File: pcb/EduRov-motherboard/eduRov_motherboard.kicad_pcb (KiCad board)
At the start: 4 copper layers, 167.7 x 124.6 mm, 65 parts, among them IC201 L6203, IC301 L6203, IC401 L6203, IC501 L6203, P101 Battery connector, P102 Ext press, P103 Ext temp, Q101 IRL540NPBF, U201 ACS723xLCTR-05AB, U301 ACS723xLCTR-05AB, U401 ACS723xLCTR-05AB, U501 ACS723xLCTR-05AB

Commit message: Update PCBs after prototyping
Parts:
- removed 2Pscrew105: Ch LED, Connectors_Terminal_Blocks:TerminalBlock_Altech_AK300-2_P5.00mm
- added P104: Ext press, Connector_JST:JST_PH_B4B-PH-K_1x04_P2.00mm_Vertical, F.Cu at (174.2, 139.1)
- added P105: Ch LED, Connector_JST:JST_PH_B4B-PH-K_1x04_P2.00mm_Vertical, F.Cu at (63.6, 87.9)
- 2Pscrew101, 2Pscrew102, 2Pscrew103, 2Pscrew104: footprint Connectors_Terminal_Blocks:TerminalBlock_Altech_AK300-2_P5.00mm -> TerminalBlock_Altech:Altech_AK300_1x02_P5.00mm_45-Degree
- IC201, IC301, IC401, IC501: footprint EduROV:MULTIWATT-11 -> SnapEDA Library:MULTIWATT-11
- P102: footprint Connectors_Terminal_Blocks:TerminalBlock_Altech_AK300-3_P5.00mm -> Connector_JST:JST_PH_B3B-PH-K_1x03_P2.00mm_Vertical
- P103: value Ext temp -> Ext press; footprint Connectors_Terminal_Blocks:TerminalBlock_Altech_AK300-3_P5.00mm -> Connector_JST:JST_PH_B3B-PH-K_1x03_P2.00mm_Vertical
- Q101: footprint TO_SOT_Packages_THT:TO-220-3_Vertical -> Package_TO_SOT_THT:TO-220-3_Vertical
- moved P103 18.4 mm to (174.2, 120.6)
- moved P102 13.5 mm to (174.2, 105.4)
- moved Q101 10.4 mm to (69.7, 82.1)
- moved D502 9.17 mm to (75.3, 40.1), turned to 270 degrees
- moved C203 8.51 mm to (209.4, 64.2), turned to 90 degrees
- moved 2Pscrew104 5.02 mm to (197.8, 46.4), turned to 90 degrees
- moved 2Pscrew101 5.02 mm to (83.8, 46.4), turned to 90 degrees
- moved 2Pscrew102 5.02 mm to (121.9, 46.4), turned to 90 degrees
- moved 2Pscrew103 5.02 mm to (159.8, 46.4), turned to 90 degrees
- moved C102 4.15 mm to (64.2, 77.5), turned to 0 degrees
- moved D501 1.61 mm to (74.9, 48.1), turned to 225 degrees
- moved R105 1.60 mm to (64.3, 71.7)
- moved R108 0.13 mm to (134.6, 74.7)
- renumbered C107 to C102
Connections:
- 2Pscrew101 pad 1: /Mot1+ -> /Mot1-
- 2Pscrew101 pad 2: /Mot1- -> /Mot1+
- 2Pscrew102 pad 1: /Mot2+ -> /Mot2-
- 2Pscrew102 pad 2: /Mot2- -> /Mot2+
- 2Pscrew103 pad 1: /Mot3+ -> /Mot3-
- 2Pscrew103 pad 2: /Mot3- -> /Mot3+
- 2Pscrew104 pad 1: /Mot4+ -> /Mot4-
- 2Pscrew104 pad 2: /Mot4- -> /Mot4+
- P101 pad 1: +Bat -> Net-(P101-Pad1)
- P101 pad 2: -Batt -> Net-(P101-Pad2)
- RaspberryPI101 pad 1: Net-(RaspberryPI101-Pad1) -> +3V3
- RaspberryPI101 pad 17: Net-(RaspberryPI101-Pad17) -> +3V3
- RaspberryPI101 pad 3: Net-(RaspberryPI101-Pad3) -> SCL
- RaspberryPI101 pad 5: Net-(RaspberryPI101-Pad5) -> SDA
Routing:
- net +3V3: track 0.00 -> 110.5 mm
- net SCL: track 0.00 -> 108.3 mm
- net SDA: track 0.00 -> 104.9 mm
- net IO_LED: track 20.2 -> 40.3 mm
- net TempMonitor: track 120.1 -> 103.1 mm
- net +Bat: track 57.6 -> 69.2 mm
- net PressMonitor: track 105.1 -> 94.2 mm
- net IO1A: track 58.7 -> 50.4 mm
- net IO1B: track 55.7 -> 49.2 mm
- net IOEN: track 188.6 -> 185.3 mm
- net /Mot1+: track 43.3 -> 46.4 mm
- net Net-(P105-Pad1): track 14.5 -> 11.6 mm
- net /Mot1-: track 27.5 -> 28.4 mm
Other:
- outline, holes or cut-outs redrawn
- board text added: "3V3 SCL SDA GND"
- board text added: "5V SIG GND"
- board text added: "Headlights"
- board text added: "I2C"
- board text added: "Revision by: Simen August Tinderholt 02.01.2020"
- board text added: "Temp"
- board text added: "V+ GND V+ GND"
- board text added: "eduROV motherboard v0.4 www.edurov.no"
- board text removed: "5V"
- board text removed: "GND"
- board text removed: "LED Channel"
- board text removed: "Revision by: Simen August Tinderholt 28.02.2020"
- board text removed: "Sig"
- board text removed: "Temperature"
- board text removed: "eduROV motherboard v0.5 www.edurov.no"

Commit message: Update schematic.
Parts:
- removed R106: 0, Resistor_THT:R_Axial_DIN0204_L3.6mm_D1.6mm_P1.90mm_Vertical
- RaspberryPI101: footprint EduROV:RaspBerry_PI -> EduRov:RaspBerry_PI
- moved R112 39.9 mm to (63.4, 89.2), turned to 0 degrees
- moved R105 20.6 mm to (63.4, 92.3)
- moved P105 13.3 mm to (61.7, 74.7), turned to 270 degrees
- moved R111 10.4 mm to (134.4, 85.1), turned to 90 degrees
- moved R108 8.96 mm to (143.6, 74.9), turned to 270 degrees
- moved R109 8.51 mm to (140.5, 85.1), turned to 90 degrees
- moved R110 6.50 mm to (137.5, 74.9), turned to 270 degrees
- moved C102 6.32 mm to (69.5, 74.0)
- moved P101 3.50 mm to (199.8, 80.5)
- moved Q101 3.39 mm to (69.3, 78.7)
- renumbered R107 to R112
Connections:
- A101 pad 17: Net-(A101-Pad17) -> +3V3
- A101 pad 19: Sense4 -> TempMonitor
- A101 pad 20: Sense3 -> PressMonitor
- A101 pad 21: Sense2 -> BattMonitor
- A101 pad 22: Sense1 -> Net-(A101-Pad22)
- A101 pad 23: Net-(A101-Pad23) -> Sense4
- A101 pad 24: BattMonitor -> Sense3
- A101 pad 25: PressMonitor -> Sense2
- A101 pad 26: TempMonitor -> Sense1
- A101 pad 27: Net-(A101-Pad27) -> +5V
- P101 pad 2: Net-(P101-Pad2) -> -Batt
- P102 pad 1: +5V -> PressMonitor
- P102 pad 2: PressMonitor -> +5V
- P103 pad 1: +5V -> TempMonitor
- P103 pad 2: TempMonitor -> +5V
- P104 pad 1: +3V3 -> SCL
- P104 pad 3: SCL -> +3V3
- P105 pad 1: Net-(P105-Pad1) -> +Bat
- P105 pad 2: +Bat -> LED-
- P105 pad 3: Net-(P105-Pad1) -> +Bat
- P105 pad 4: +Bat -> LED-
- Q101 pad 2: Net-(P105-Pad1) -> LED-
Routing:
- net +3V3: track 110.5 -> 10.5 mm
- net +Bat: track 69.2 -> 47.4 mm, vias 5 -> 2
- net TempMonitor: track 103.1 -> 86.7 mm
- net Sense1: track 45.6 -> 32.3 mm
- net IOEN: track 185.3 -> 197.3 mm
- net Net-(P105-Pad1): track 11.6 -> 0.00 mm
- net -Batt: track 62.4 -> 72.6 mm
- net Sense3: track 44.8 -> 54.9 mm
- net SCL: track 108.3 -> 117.6 mm
- net SDA: track 104.9 -> 111.4 mm
- net PressMonitor: track 94.2 -> 89.0 mm
- net Sense2: track 14.1 -> 17.4 mm
- net Net-(A101-Pad27): track 2.95 -> 0.00 mm
- net +5V: track 15.9 -> 18.8 mm
- net BattMonitor: track 46.2 -> 43.4 mm
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- added copper zone on F.Cu, net +3V3
- added copper zone on F.Cu, net +Bat
- added copper zone on B.Cu, net LED-
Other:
- board text added: "Battery Connector"
- board text added: "Battery Level"
- board text added: "Option A: Solder socket header here"
- board text added: "Option B: Solder pins here"
- board text added: "Revision by: Simen August Tinderholt 14.04.2021"
- board text added: "SCL SDA 3V3 GND"
- board text added: "SIG 5V GND"
- board text added: "V+ GND"
- board text removed: "3V3 SCL SDA GND"
- board text removed: "5V SIG GND"
- board text removed: "Battery Monitoring"
- board text removed: "Revision by: Simen August Tinderholt 02.01.2020"
- board text removed: "Short if not powering Arduino with USB"
- board text removed: "V+ GND V+ GND"

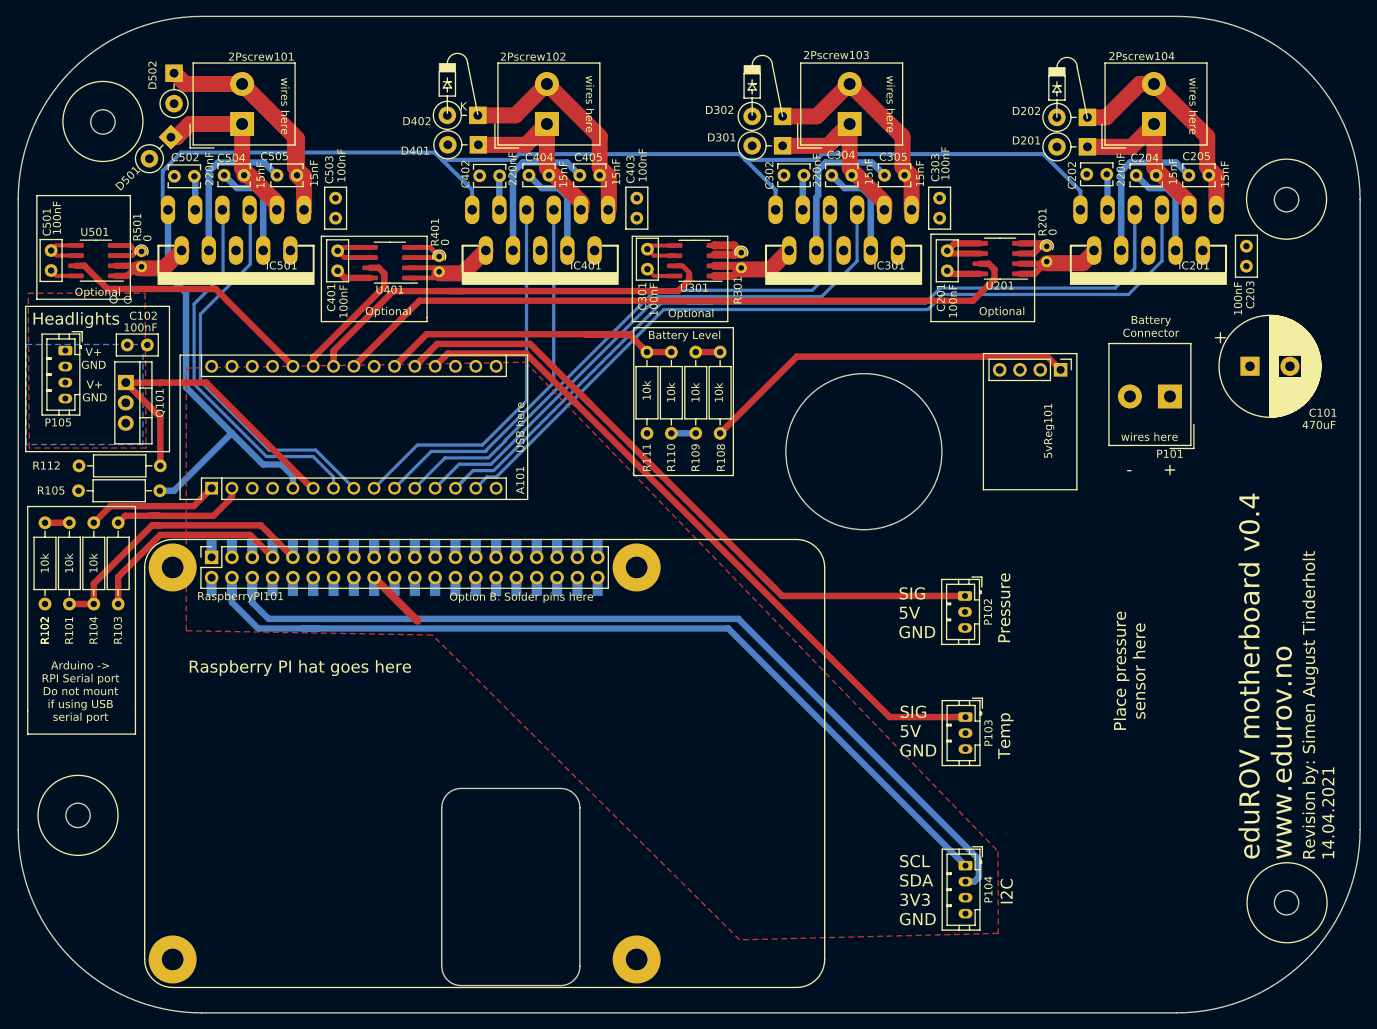
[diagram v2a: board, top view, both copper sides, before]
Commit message: Update footprints with models
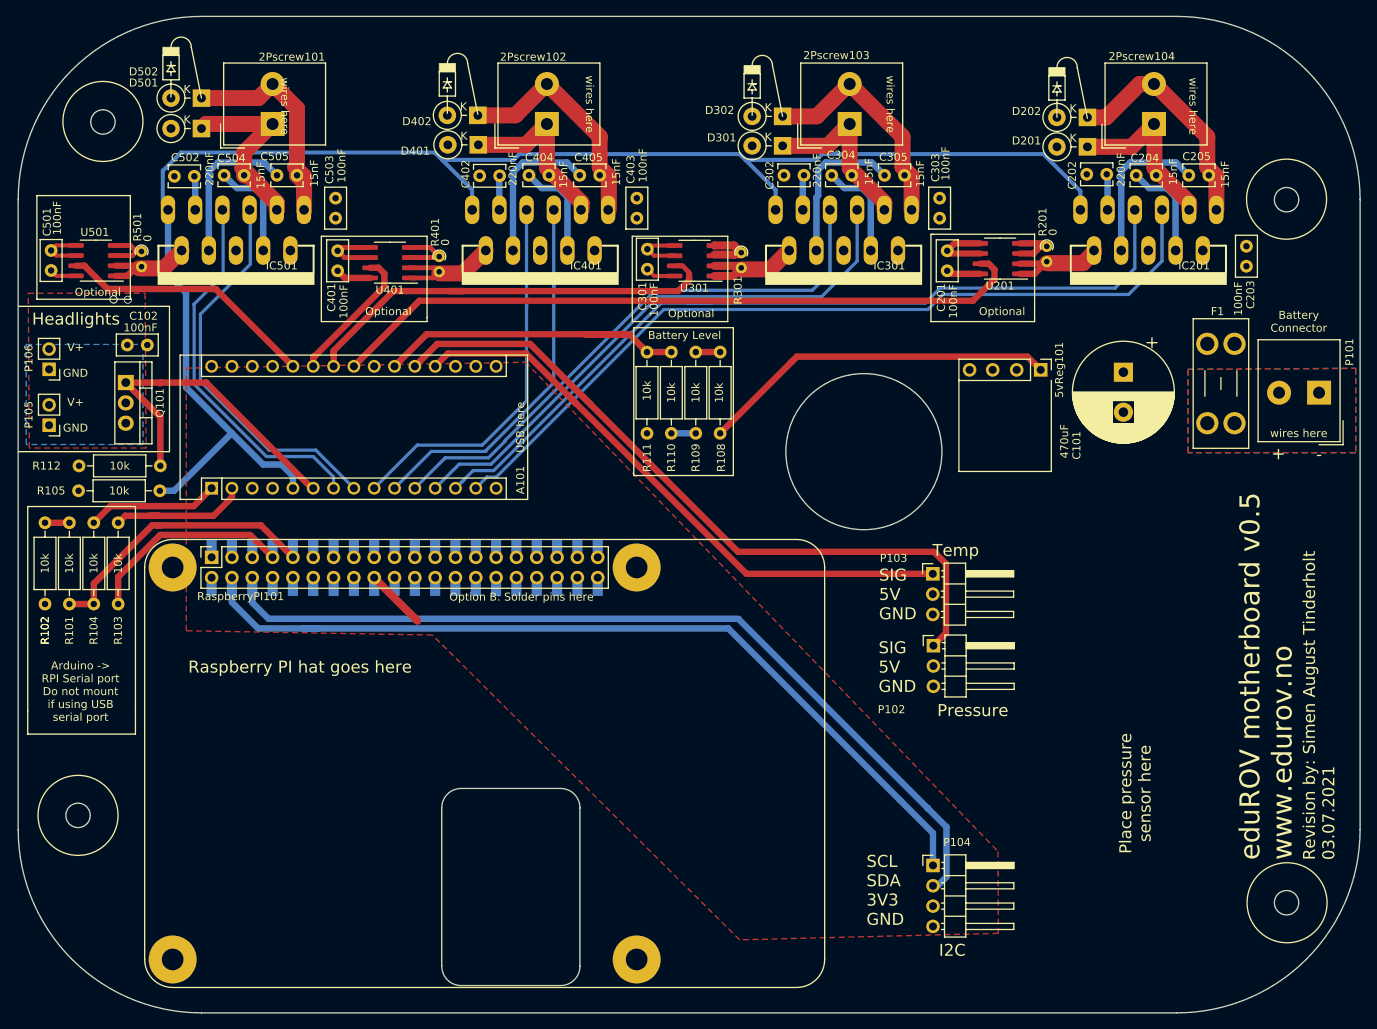
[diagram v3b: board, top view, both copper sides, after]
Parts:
- added F1: Fuse, Fuse:Fuseholder_Blade_Mini_Keystone_3568, F.Cu at (204.5, 83.8)
- added P106: HeadLight, Connector_PinHeader_2.54mm:PinHeader_1x02_P2.54mm_Vertical, F.Cu at (59.7, 77.1)
- 5vReg101: footprint Connector_PinHeader_2.54mm:PinHeader_1x04_P2.54mm_Vertical -> EduRov:iFlight_Micro
- IC201, IC301, IC401, IC501: footprint SnapEDA Library:MULTIWATT-11 -> EduRov:MULTIWATT-11
- P102, P103: footprint Connector_JST:JST_PH_B3B-PH-K_1x03_P2.00mm_Vertical -> Connector_PinHeader_2.54mm:PinHeader_1x03_P2.54mm_Horizontal
- P104: footprint Connector_JST:JST_PH_B4B-PH-K_1x04_P2.00mm_Vertical -> Connector_PinHeader_2.54mm:PinHeader_1x04_P2.54mm_Horizontal
- P105: value Ch LED -> HeadLight; footprint Connector_JST:JST_PH_B4B-PH-K_1x04_P2.00mm_Vertical -> Connector_PinHeader_2.54mm:PinHeader_1x02_P2.54mm_Vertical
- moved P101 18.6 mm to (218.4, 80.0)
- moved P103 18.4 mm to (170.2, 102.6), turned to 0 degrees
- moved C101 15.8 mm to (194.0, 77.4), turned to 270 degrees
- moved P105 9.55 mm to (59.7, 84.1), turned to 180 degrees
- moved P102 7.37 mm to (170.2, 111.6), turned to 0 degrees
- moved D502 4.63 mm to (78.7, 43.2), turned to 180 degrees
- moved P104 4.06 mm to (170.2, 139.1), turned to 0 degrees
- moved D501 3.96 mm to (78.7, 47.0), turned to 180 degrees
- moved 2Pscrew101 3.81 mm to (87.6, 46.4)
- moved 5vReg101 2.49 mm to (183.6, 77.2)
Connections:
- C101 pad 1: -Batt -> +Bat
- C101 pad 2: +Bat -> -Batt
- P101 pad 1: Net-(P101-Pad1) -> -Batt
- P101 pad 2: -Batt -> Net-(F1-Pad1)
- P105 pad 1: +Bat -> /LED-
- P105 pad 2: LED- -> +Bat
- Q101 pad 2: LED- -> /LED-
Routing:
- net /Mot1+: track 46.4 -> 32.8 mm
- net TempMonitor: track 86.7 -> 75.2 mm
- net PressMonitor: track 89.0 -> 92.7 mm
- net +Bat: track 47.4 -> 44.9 mm
- net /Mot1-: track 28.4 -> 30.4 mm
- net SCL: track 117.6 -> 115.9 mm
- net SDA: track 111.4 -> 109.9 mm
- net -Batt: track 72.6 -> 74.0 mm
- added copper zone on B.Cu, net /LED-
- added copper zone on B.Cu, net Net-(F1-Pad1)
- added copper zone on F.Cu, net Net-(F1-Pad1)
- removed copper zone on B.Cu, net LED-
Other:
- board text added: "Revision by: Simen August Tinderholt 03.07.2021"
- board text added: "eduROV motherboard v0.5 www.edurov.no"
- board text removed: "Revision by: Simen August Tinderholt 14.04.2021"
- board text removed: "eduROV motherboard v0.4 www.edurov.no"

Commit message: Motherboard updates
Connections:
- A101 pad 17: +3V3 -> Net-(A101-Pad17)
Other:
- board text added: "Lift"
- board text added: "Port"
- board text added: "Starboard"
- board text added: "eduROV motherboard v0.6 www.edurov.no"
- board text removed: "eduROV motherboard v0.5 www.edurov.no"
